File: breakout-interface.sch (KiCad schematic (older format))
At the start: 3 parts

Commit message: Schematic nearly done
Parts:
- added C? (x2): 82p, symbol C
- added C? (x2): 10u, symbol C
- added C? (x2): 4.7u, symbol C
- added D? (x2): MBR0540, symbol D_Schottky
- added IC? (x2): LM7233, symbol LM7233
- added IC? (x2): OPA454, symbol OPA454
- added JP?: Jumper_NO_Small, symbol Jumper_NO_Small
- added L? (x2): INDUCTOR, symbol INDUCTOR
- added P1: USB_OTG, Connect:USB_Micro-B, symbol USB_OTG
- added P?: CONN_02X04, symbol CONN_02X04
- added P? (x4): CONN_01X04, symbol CONN_01X04
- added R? (x2): 47K, symbol R
- added R? (x2): 309K, symbol R
- added R? (x2): 12K, symbol R
- added R? (x2): 1M, symbol R
- added R? (x6): 91K, symbol R
- added R? (x6): 10K, symbol R
- added R? (x2): 10R, symbol R
- added R? (x2): 4.7K, symbol R
- added U?: 24C16, symbol 24C16
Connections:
- net AIN0.0: now also R?.1, R?.2
- net AIN0.1: now also R?.1, R?.2
- net AIN0.2: now also R?.1, R?.2
- net AIN0.3: now also R?.1, R?.2
- net AOUT0.0: now also IC?.3 (+)
- net AOUT0.1: now also IC?.3 (+)
- net GND: now also C?.1, C?.2, C?.2, C?.2, C?.2, D?.1 (K), IC?.2 (GND), P1.5 (GND), P1.6 (shield), P?.1 (P1), P?.2 (P2), P?.3 (P3), P?.3 (P3), P?.4 (P4), P?.4 (P4), P?.5 (P5), P?.6 (P6), P?.7 (P7), P?.8 (P8), R?.1, R?.1, R?.1, R?.1, R?.1, R?.1, R?.2, R?.2, U?.4 (GND)
- new net: D?.2 (A), IC?.1 (SW), L?.1 (x2)
- new net: C?.1, IC?.3 (FB), R?.1, R?.1 (x2)
- new net: IC?.4 (~SHDN), R?.2 (x2)
- new net: IC?.2 (-), R?.2, R?.2 (x2)
- new net: IC?.6, R?.1, R?.2 (x2)
- new net: IC?.8, R?.2 (x2)
- new net: P?.1 (P1), R?.1
- new net: P?.1 (P1), R?.2
- new net: P?.2 (P2), R?.2
- new net: P?.3 (P3), R?.2
- new net: P?.4 (P4), R?.2
- new net: JP?.2, U?.7 (WP)
- new net +33V: C?.1, C?.2, D?.1 (K), IC?.7 (V+), IC?.7 (V+), P?.1 (P1), P?.2 (P2), P?.3 (P3), P?.4 (P4), R?.1, R?.1, R?.2
- new net -33V: C?.2, IC?.1, IC?.1, IC?.2 (GND), IC?.4 (V-), IC?.4 (V-), P?.1 (P1), P?.2 (P2), P?.3 (P3), P?.4 (P4), R?.2
- new net 5V: C?.1, C?.1, IC?.5 (Vin), IC?.5 (Vin), L?.2, L?.2, P1.1 (VCC), R?.1, R?.1
- new net DIGITAL_EXT: JP?.1, R?.1, R?.1, U?.1 (A0), U?.2 (A1), U?.3 (A2), U?.8 (VCC)
- new net I2C0.SCL: R?.2, U?.6 (SCL)
- new net I2C0.SDA: R?.2, U?.5 (SDA)
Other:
- note added: "USB port for power. \n+-35V or such at 10mA per channel means rougly 700mW output power.\nAdd losses for the SMPS and rougly 1W power needed, 2W with 2 outputs.\nMore then the 5V can deliver, hence an external input."
- note added: "Used as an ID\nCan be flashed once with an ID, the Box0\ncan then read the ID and know what type\nof shield is connected"
- moved on the sheet: C1, C2, C3

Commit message: Started on PCB
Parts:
- added C10, C11, C12, C13, C14: 100n, rik_footprints:0603, symbol C
- C1, C2, C3: footprint Capacitors_SMD:C_0603_HandSoldering -> rik_footprints:0603
- C4, C5, C8, C9: renamed from C?; footprint (none) -> rik_footprints:0805
- C6, C7: renamed from C?; footprint (none) -> rik_footprints:0603
- D1, D2: renamed from D?; footprint (none) -> Diodes_SMD:SOD-123
- IC1, IC2: renamed from IC?; value LM7233 -> LM2733; footprint (none) -> TO_SOT_Packages_SMD:SOT-23-5
- IC3, IC4: renamed from IC?; footprint (none) -> rik_footprints:SOIC-8-3.9*4.9mm_HP_to_P4
- JP1: renamed from JP?; footprint (none) -> Capacitors_SMD:C_0201
- L1, L2: renamed from L?; value INDUCTOR -> 10u; footprint (none) -> rik_footprints:0805
- P4: renamed from P?; footprint (none) -> Pin_Headers:Pin_Header_Straight_2x04
- P5, P6, P7, P8: renamed from P?; footprint (none) -> Pin_Headers:Pin_Header_Straight_1x04
- R1, R10, R11, R12, R13, R14, R15, R16, R17, R18, R19, R2, R20, R21, R22, R23, R24, R3, R4, R5, R6, R7, R8, R9: renamed from R?; footprint (none) -> rik_footprints:0603
- U1: renamed from U?; footprint (none) -> Housings_SOIC:SOIC-8_3.9x4.9mm_Pitch1.27mm
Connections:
- net +33V: now also C12.1, C13.1
- net -33V: now also C10.1, C11.1
- net DIGITAL_EXT: now also C14.1
- net GND: now also C10.2, C11.2, C12.2, C13.2, C14.2
- net at R13.1: now also P4.2 (P2)

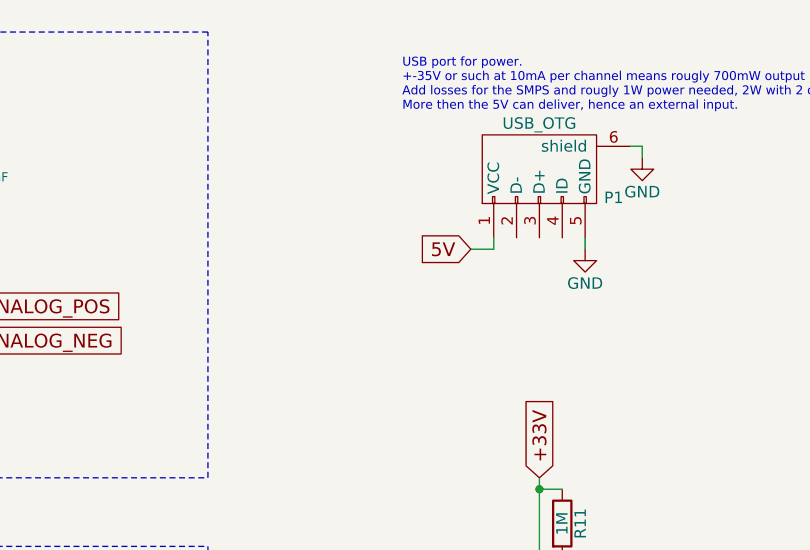
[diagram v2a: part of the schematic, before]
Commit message: fixed the wrongly connected VREF
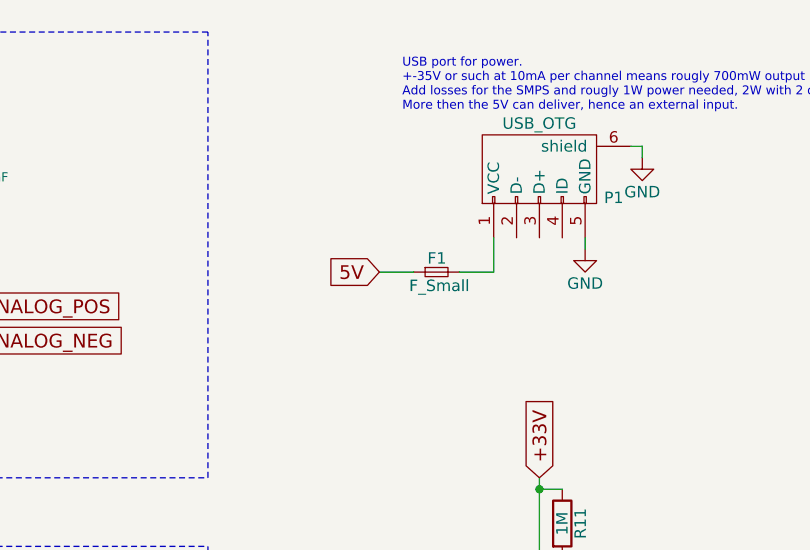
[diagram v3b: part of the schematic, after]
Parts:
- added F1: F_Small, SMD_Packages:SMD-1210_Pol, symbol F_Small
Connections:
- net 5V: now also F1.1; no longer P1.1 (VCC)
- new net: F1.2, P1.1 (VCC)
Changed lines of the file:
@@
 	1    0    0    -1
 $EndComp
-Text GLabel 5300 1600 0    60   Input ~ 0
+Text GLabel 4900 1700 0    60   Input ~ 0
 5V
 $Comp
@@
 Wire Wire Line
 	6050 1150 6000 1150
-Wire Wire Line
-	5300 1600 5400 1600
-Wire Wire Line
-	5400 1600 5400 1550
 Wire Wire Line
 	1400 3450 1950 3450
@@
 Wire Wire Line
 	7400 3500 7250 3500
+$Comp
+L F_Small F1
+U 1 1 585C4AFB
+P 5150 1700
+F 0 "F1" H 5110 1760 50  0000 L CNN
+F 1 "F_Small" H 5030 1640 50  0000 L CNN
+F 2 "SMD_Packages:SMD-1210_Pol" H 5150 1700 50  0001 C CNN
+F 3 "" H 5150 1700 50  0000 C CNN
+	1    5150 1700
+	1    0    0    -1
+$EndComp
+Wire Wire Line
+	5400 1550 5400 1700
+Wire Wire Line
+	5400 1700 5250 1700
+Wire Wire Line
+	5050 1700 4900 1700
 $EndSCHEMATC
